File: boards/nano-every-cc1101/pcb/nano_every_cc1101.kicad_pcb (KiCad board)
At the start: 2 copper layers, 100 x 100 mm, 81 parts, among them J1 SMA, J2 SMA, J3 Breakout 1-15, J4 Breakout 16-30, U1 CC1101RGPR, U2 AP2112K-3.3, U3 TXS0108EPWR, U501 CC1101RGPR, Y1 26MHz, Y501 26MHz

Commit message: nano-every-cc1101: final openEMS-tuned antennas, T-match values, fab outputs
- 433/868/915 MHz inverted-F antennas tuned in a full-board openEMS model
  (all four antennas present); 315 MHz meandered IFA with a 47 nH loading
  coil chosen from a 2-port model (feed + coil gap)
- T-match values from design_match.py with realistic part Q; simulated
  S11: 433 -15.9 dB, 315 -18.7 dB, 868 -31 dB, 915 -26 dB, each -10 dB band
  covering its ISM band
- BOM with exact Murata MPNs for match parts; JLCPCB BOM/CPL, Gerbers,
  DRC (0 errors, 0 unconnected pads), netlist regenerated
- Docs: README, antenna README + results, design notes, assembly/bring-up

Co-Authored-By: Claude Opus 5.5 <noreply@anthropic.com>
Claude-Session: https://claude.ai/code/session_019aUkwoH7eUuCGWSrK9KSBc
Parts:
- C301: value DNP -> 56nH
- C311: value DNP -> 27nH
- C321: value DNP -> 3.6pF
- C331: value DNP -> 2.4pF
- L311: value 0R -> 6.8pF
- L321: value 0R -> 6.2pF
- L331: value 0R -> 2.7pF
- L402: value 56nH -> 47nH
- R301: value 0R -> 16pF
- R311, R331: value DNP -> DNP (0R to use)
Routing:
- net 3V3: track 44.8 -> 117.8 mm, vias 8 -> 10
- net D13_SCK: track 3.40 -> 65.8 mm, vias 0 -> 1
- net D12_MISO: track 3.40 -> 63.5 mm, vias 0 -> 1
- net D11_MOSI: track 3.40 -> 58.5 mm, vias 0 -> 1
- net D10: track 3.40 -> 55.4 mm, vias 0 -> 1
- net D9: track 3.40 -> 52.0 mm, vias 0 -> 1
- net SI: track 3.04 -> 51.1 mm, vias 0 -> 3
- net SO: track 3.03 -> 50.4 mm
- net SCLK: track 1.83 -> 44.7 mm, vias 0 -> 2
- net D3: track 3.40 -> 40.3 mm, vias 0 -> 1
- net D4: track 3.40 -> 39.1 mm, vias 0 -> 1
- net +5V: track 12.9 -> 46.8 mm
- net D2: track 3.40 -> 37.3 mm
- net GDO2_A: track 0.89 -> 28.1 mm, vias 0 -> 2
- net CSN_B: track 0.86 -> 25.0 mm, vias 0 -> 2
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
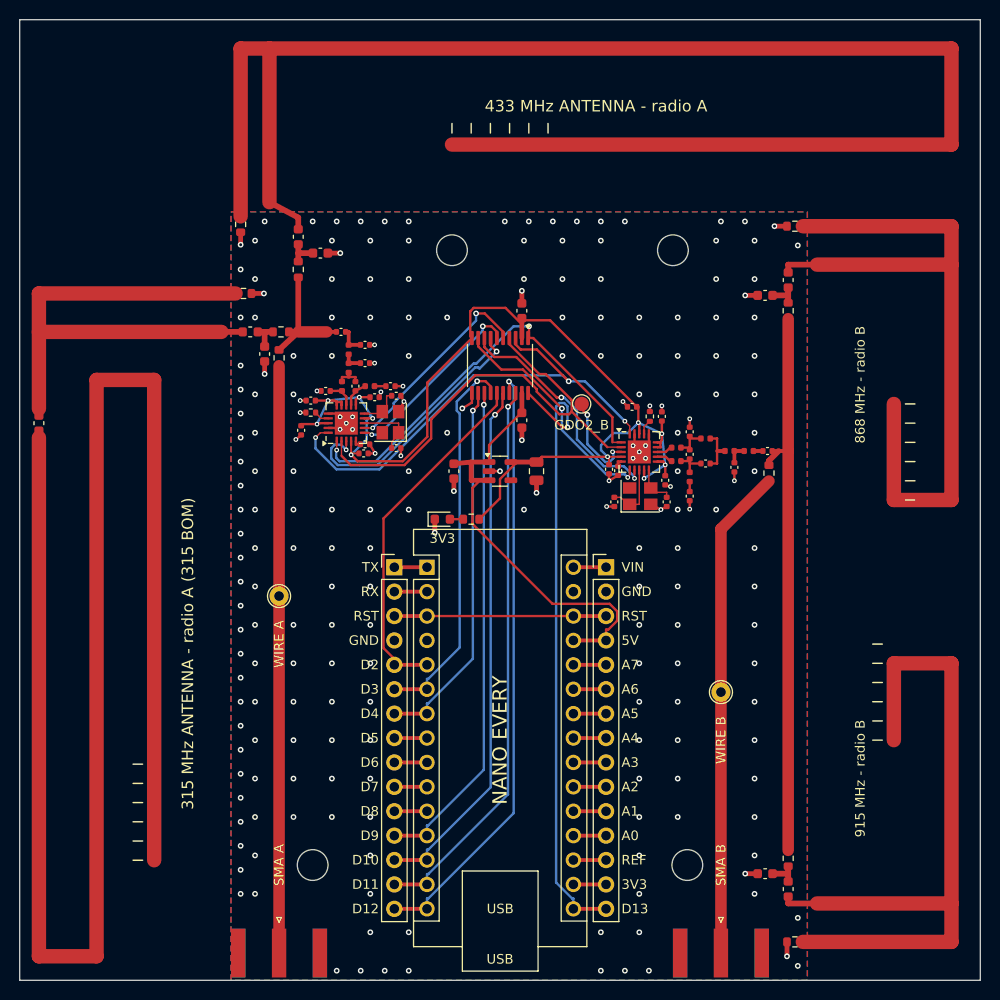
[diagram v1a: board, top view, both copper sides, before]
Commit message: nano-every-cc1101: tunable antennas covering every CC1101 frequency
Every printed antenna now has a series tuning element in its arm (L401/
L402/L404/L405) in addition to its T-match. A 2-port openEMS model of the
full board per antenna (feed + tuning gap) gives Zin for any tuning part,
and tune.py picks tuning part + T-match (E12/E24 0603, with losses) for
every MHz: 300-348 MHz (315 antenna), 387-464 (433), 779-880 (868),
870-928 (915), S11 < -15 dB throughout. Per-MHz tables, coverage plot,
whip-length table; board defaults regenerated from the new model; Gerbers,
BOM/CPL and docs updated. Replaces design_match.py / choose_load.py.

Co-Authored-By: Claude Opus 5.5 <noreply@anthropic.com>
Claude-Session: https://claude.ai/code/session_019aUkwoH7eUuCGWSrK9KSBc
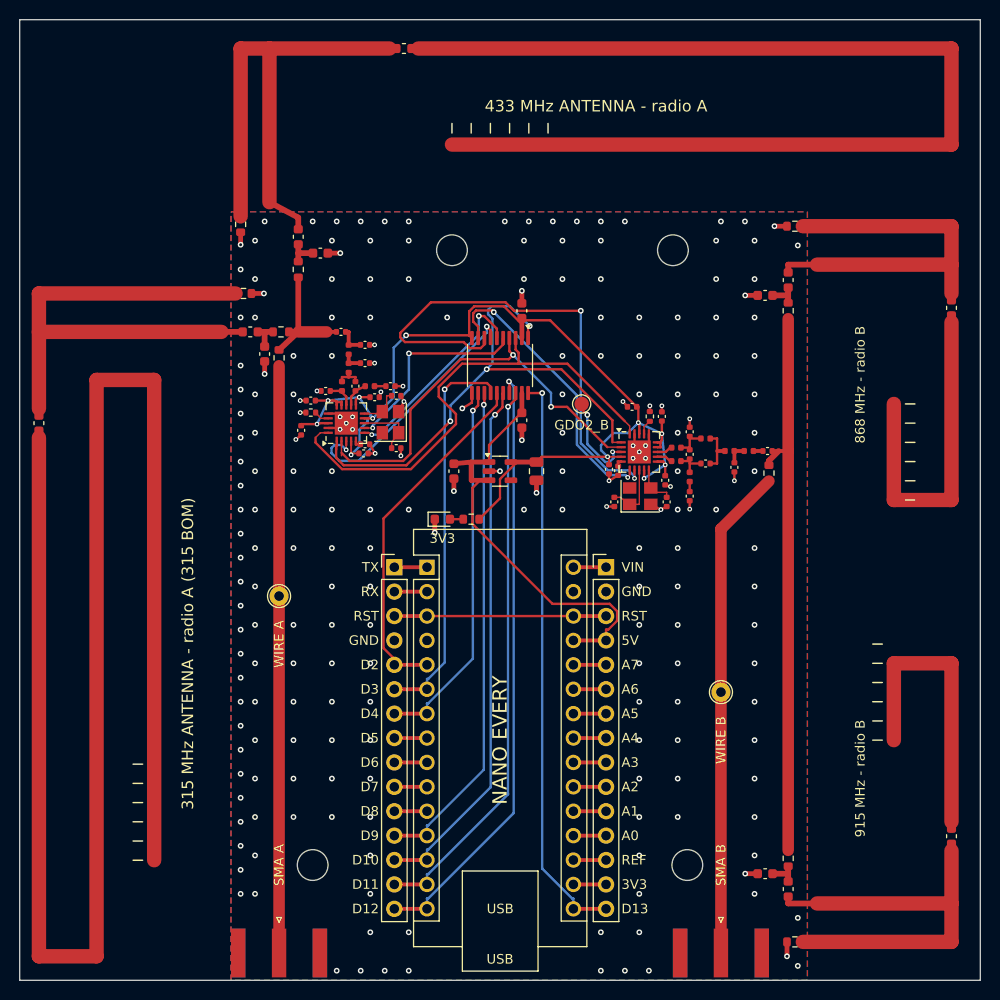
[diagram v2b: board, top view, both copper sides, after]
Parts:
- added L401: 51pF, Inductor_SMD:L_0603_1608Metric, F.Cu at (140.0, 103.0)
- added L404: 0R, Inductor_SMD:L_0603_1608Metric, F.Cu at (197.0, 130.0)
- added L405: 0R, Inductor_SMD:L_0603_1608Metric, F.Cu at (197.0, 185.0)
- C301: value 56nH -> 1.1pF
- C311: value 27nH -> 10pF
- C331: value 2.4pF -> 2.7pF
- L301: value 0R -> 5.1pF
- L311: value 6.8pF -> 0R
- L402: value 47nH -> 39nH
- R301: value 16pF -> 0R
- R311: value DNP (0R to use) -> DNP (2.7pF to use)
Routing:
- net FEED_433: track 174.1 -> 54.3 mm
- net ARM_433: track 0.00 -> 118.2 mm
- net FEED_868: track 77.8 -> 41.0 mm
- net ARM_868: track 0.00 -> 35.2 mm
- net FEED_915: track 76.2 -> 43.4 mm
- net ARM_915: track 0.00 -> 31.2 mm
- net CSN_B: track 25.0 -> 52.9 mm
- net SCLK: track 44.7 -> 55.1 mm, vias 2 -> 3
- net GDO0_B: track 24.2 -> 30.1 mm
- net D13_SCK: track 65.8 -> 60.0 mm
- net SO: track 50.4 -> 45.1 mm, vias 0 -> 2
- net 3V3: track 117.8 -> 113.3 mm, vias 10 -> 11
- net GDO0_A: track 19.7 -> 21.6 mm
- net D3: track 40.3 -> 41.3 mm
- net GDO2_A: track 28.1 -> 27.3 mm
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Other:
- board text added: "ANY FREQUENCY 300-348/387-464/779-928 MHz:"
- board text added: "fit tune L40x + R3x1/C3x1/L3x1 per tuning.md"
- board text added: "whip for SMA/wire: L(mm) = 71250 / f(MHz)"
- board text removed: "wire whip: 164mm@433 226@315 82@868 78@915"
